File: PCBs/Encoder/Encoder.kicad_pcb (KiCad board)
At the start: 2 copper layers, 6 x 25 mm, 3 parts, among them J1 Conn_01x06_Male, U1 AS5047D

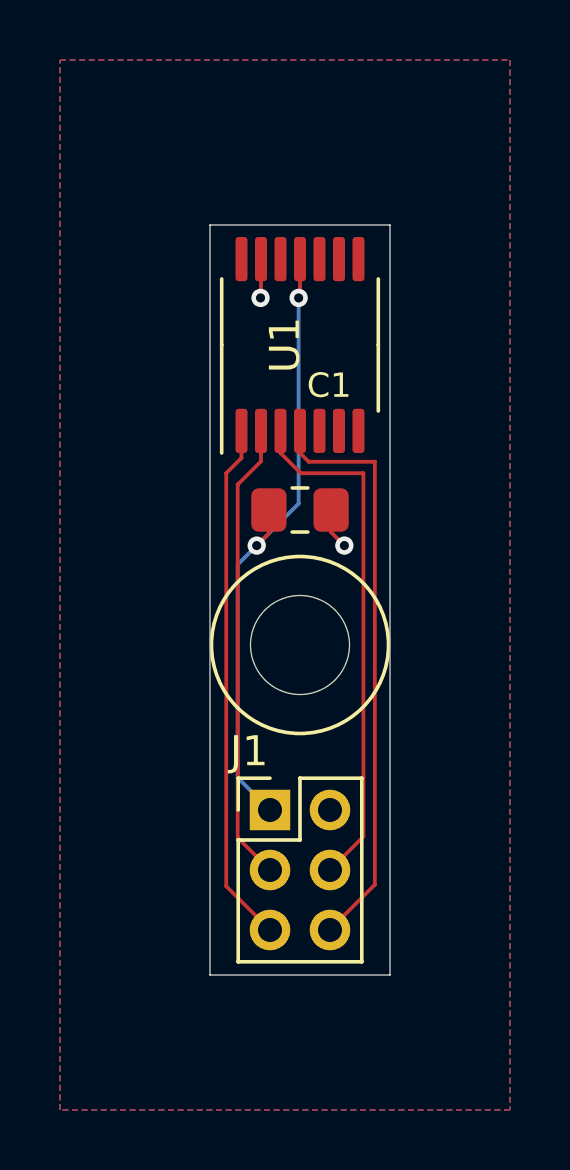
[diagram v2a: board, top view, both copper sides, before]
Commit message: encoder PCB update
datum relief and traces on bottom
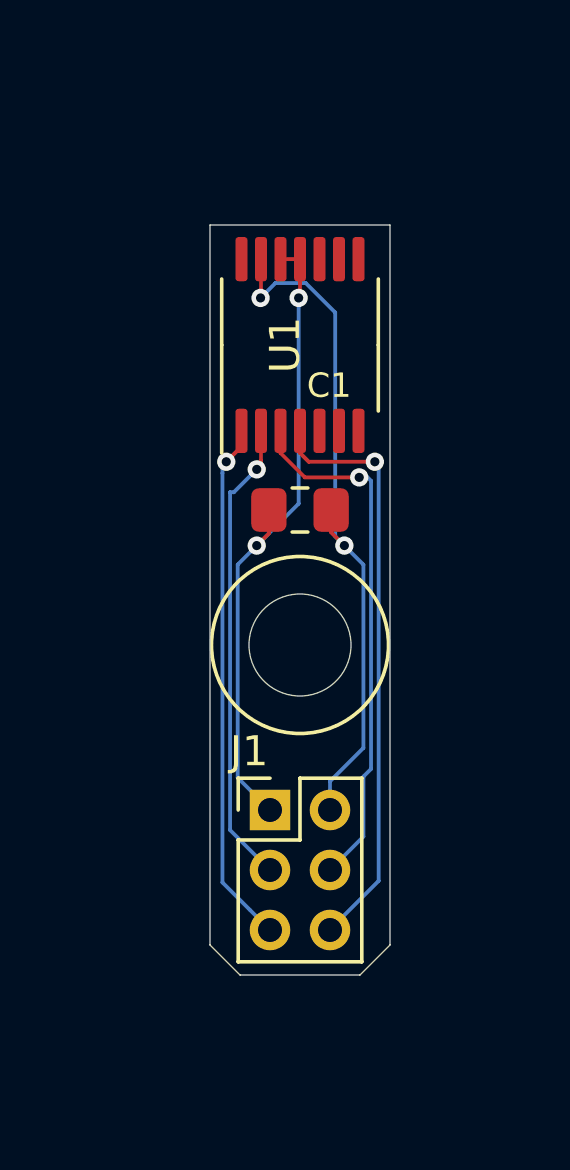
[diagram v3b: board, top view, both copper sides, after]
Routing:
- net GND: track 2.67 -> 23.2 mm
- net +3V3: track 21.0 -> 21.7 mm
- net CLK: track 15.4 -> 15.7 mm, vias 0 -> 1
- net MISO: track 17.5 -> 17.6 mm, vias 0 -> 1
- net CS: track 17.5 -> 17.6 mm, vias 0 -> 1
- net MOSI: track 19.6 -> 19.7 mm, vias 0 -> 1
- removed copper zone on F.Cu, net +3V3
- removed copper zone on B.Cu, net GND
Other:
- outline, holes or cut-outs redrawn
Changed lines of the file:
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@@
   (general
     (thickness 1.6)
-    (drawings 12)
-    (tracks 36)
+    (drawings 14)
+    (tracks 59)
     (zones 0)
     (modules 3)
@@
     (44 Edge.Cuts user)
     (45 Margin user)
-    (46 B.CrtYd user)
-    (47 F.CrtYd user)
+    (46 B.CrtYd user hide)
+    (47 F.CrtYd user hide)
     (48 B.Fab user hide)
     (49 F.Fab user)
@@
       (drillshape 0)
       (scaleselection 1)
-      (outputdirectory "/Output/"))
+      (outputdirectory "./Output/"))
   )
   (net 0 "")
@@
     )
   )
+  (gr_line (start 146 105.5) (end 145 104.5) (layer Edge.Cuts) (width 0.0254))
+  (gr_line (start 150 105.5) (end 151 104.5) (layer Edge.Cuts) (width 0.0254))
   (dimension 14 (width 0.15) (layer F.Fab)
     (gr_text "14.000 mm" (at 154.6152 87.5 90) (layer F.Fab)
@@
     (arrow2b (pts (xy 145 78.5) (xy 146.126504 77.913579)))
   )
-  (gr_line (start 145 105.5) (end 145 80.5) (layer Edge.Cuts) (width 0.0254))
-  (gr_line (start 151 105.5) (end 145 105.5) (layer Edge.Cuts) (width 0.0254))
-  (gr_line (start 151 80.5) (end 151 105.5) (layer Edge.Cuts) (width 0.0254))
+  (gr_line (start 145 104.5) (end 145 80.5) (layer Edge.Cuts) (width 0.0254))
+  (gr_line (start 150 105.5) (end 146 105.5) (layer Edge.Cuts) (width 0.0254))
+  (gr_line (start 151 80.5) (end 151 104.5) (layer Edge.Cuts) (width 0.0254))
   (gr_circle (center 148 94.5) (end 150.95 94.5) (layer F.SilkS) (width 0.12))
-  (gr_circle (center 148 94.5) (end 149.65 94.5) (layer Edge.Cuts) (width 0.0254))
+  (gr_circle (center 148 94.5) (end 149.7 94.5) (layer Edge.Cuts) (width 0.0254))
   (gr_line (start 145 80.5) (end 151 80.5) (layer Edge.Cuts) (width 0.0254))
   (via (at 146.685 82.931) (size 0.6096) (drill 0.3048) (layers F.Cu B.Cu) (net 1))
@@
   (segment (start 149.0375 90.7445) (end 149.479 91.186) (width 0.127) (layer F.Cu) (net 1))
   (segment (start 149.0375 90) (end 149.0375 90.7445) (width 0.127) (layer F.Cu) (net 1))
+  (segment (start 149.479 91.186) (end 150.114 91.821) (width 0.127) (layer B.Cu) (net 1))
+  (segment (start 149 99.045406) (end 149 100) (width 0.127) (layer B.Cu) (net 1))
+  (segment (start 150.114 97.931406) (end 149 99.045406) (width 0.127) (layer B.Cu) (net 1))
+  (segment (start 150.114 91.821) (end 150.114 97.931406) (width 0.127) (layer B.Cu) (net 1))
+  (segment (start 147.180301 82.435699) (end 146.685 82.931) (width 0.127) (layer B.Cu) (net 1))
+  (segment (start 148.192745 82.435699) (end 147.180301 82.435699) (width 0.127) (layer B.Cu) (net 1))
+  (segment (start 149.174201 83.417155) (end 148.192745 82.435699) (width 0.127) (layer B.Cu) (net 1))
+  (segment (start 149.174201 90.881201) (end 149.174201 83.417155) (width 0.127) (layer B.Cu) (net 1))
+  (segment (start 149.479 91.186) (end 149.174201 90.881201) (width 0.127) (layer B.Cu) (net 1))
   (via (at 147.955 82.931) (size 0.6096) (drill 0.3048) (layers F.Cu B.Cu) (net 2))
   (segment (start 148 82.886) (end 147.955 82.931) (width 0.127) (layer F.Cu) (net 2))
@@
   (segment (start 145.923 98.923) (end 147 100) (width 0.127) (layer B.Cu) (net 2))
   (segment (start 145.923 91.821) (end 145.923 98.923) (width 0.127) (layer B.Cu) (net 2))
-  (segment (start 146.05 87.3625) (end 146.05 88.265) (width 0.127) (layer F.Cu) (net 3))
-  (segment (start 146.05 88.265) (end 145.542 88.773) (width 0.127) (layer F.Cu) (net 3))
-  (segment (start 145.542 102.542) (end 147 104) (width 0.127) (layer F.Cu) (net 3))
-  (segment (start 145.542 88.773) (end 145.542 102.542) (width 0.127) (layer F.Cu) (net 3))
-  (segment (start 145.923 100.923) (end 147 102) (width 0.127) (layer F.Cu) (net 4))
-  (segment (start 145.923 89.154) (end 145.923 100.923) (width 0.127) (layer F.Cu) (net 4))
-  (segment (start 146.7 88.377) (end 145.923 89.154) (width 0.127) (layer F.Cu) (net 4))
+  (segment (start 147.35 81.6375) (end 148 81.6375) (width 0.127) (layer F.Cu) (net 2))
+  (segment (start 145.414989 102.414989) (end 146.325001 103.325001) (width 0.127) (layer B.Cu) (net 3))
+  (segment (start 146.325001 103.325001) (end 147 104) (width 0.127) (layer B.Cu) (net 3))
+  (via (at 145.542 88.392) (size 0.6096) (drill 0.3048) (layers F.Cu B.Cu) (net 3))
+  (segment (start 146.05 87.884) (end 145.542 88.392) (width 0.127) (layer F.Cu) (net 3))
+  (segment (start 146.05 87.3625) (end 146.05 87.884) (width 0.127) (layer F.Cu) (net 3))
+  (segment (start 145.414989 88.519011) (end 145.414989 88.773011) (width 0.127) (layer B.Cu) (net 3))
+  (segment (start 145.542 88.392) (end 145.414989 88.519011) (width 0.127) (layer B.Cu) (net 3))
+  (segment (start 145.414989 88.773011) (end 145.414989 102.414989) (width 0.127) (layer B.Cu) (net 3))
+  (segment (start 145.669 100.669) (end 147 102) (width 0.127) (layer B.Cu) (net 4))
+  (segment (start 145.669 89.408) (end 145.669 100.669) (width 0.127) (layer B.Cu) (net 4))
   (segment (start 146.7 87.3625) (end 146.7 88.377) (width 0.127) (layer F.Cu) (net 4))
-  (segment (start 150.114 88.773) (end 150.114 98.886) (width 0.127) (layer F.Cu) (net 5))
-  (segment (start 148.023 88.773) (end 150.114 88.773) (width 0.127) (layer F.Cu) (net 5))
-  (segment (start 147.35 88.1) (end 148.023 88.773) (width 0.127) (layer F.Cu) (net 5))
+  (via (at 146.558 88.646) (size 0.6096) (drill 0.3048) (layers F.Cu B.Cu) (net 4))
+  (segment (start 146.7 88.504) (end 146.558 88.646) (width 0.127) (layer F.Cu) (net 4))
+  (segment (start 146.7 88.377) (end 146.7 88.504) (width 0.127) (layer F.Cu) (net 4))
+  (segment (start 145.796 89.408) (end 145.669 89.408) (width 0.127) (layer B.Cu) (net 4))
+  (segment (start 146.558 88.646) (end 145.796 89.408) (width 0.127) (layer B.Cu) (net 4))
+  (via (at 149.974144 88.912856) (size 0.6096) (drill 0.3048) (layers F.Cu B.Cu) (net 5))
+  (segment (start 148.162856 88.912856) (end 149.974144 88.912856) (width 0.127) (layer F.Cu) (net 5))
+  (segment (start 147.35 88.1) (end 148.162856 88.912856) (width 0.127) (layer F.Cu) (net 5))
   (segment (start 147.35 87.3625) (end 147.35 88.1) (width 0.127) (layer F.Cu) (net 5))
-  (segment (start 150.114 100.886) (end 149 102) (width 0.127) (layer F.Cu) (net 5))
-  (segment (start 150.114 98.886) (end 150.114 100.886) (width 0.127) (layer F.Cu) (net 5))
-  (segment (start 150.495 102.489) (end 149 103.984) (width 0.127) (layer F.Cu) (net 6))
-  (segment (start 150.495 88.392) (end 150.495 102.489) (width 0.127) (layer F.Cu) (net 6))
-  (segment (start 148.292 88.392) (end 150.495 88.392) (width 0.127) (layer F.Cu) (net 6))
+  (segment (start 150.114 100.886) (end 149 102) (width 0.127) (layer B.Cu) (net 5))
+  (segment (start 150.114 98.886) (end 150.114 100.886) (width 0.127) (layer B.Cu) (net 5))
+  (segment (start 150.368 98.632) (end 150.114 98.886) (width 0.127) (layer B.Cu) (net 5))
+  (segment (start 150.368 89.027) (end 150.368 98.632) (width 0.127) (layer B.Cu) (net 5))
+  (segment (start 150.114 88.773) (end 150.368 89.027) (width 0.127) (layer B.Cu) (net 5))
   (segment (start 148 88.1) (end 148.292 88.392) (width 0.127) (layer F.Cu) (net 6))
   (segment (start 148 87.3625) (end 148 88.1) (width 0.127) (layer F.Cu) (net 6))
-  (zone (net 2) (net_name +3V3) (layer F.Cu) (hatch edge 0.508)
-    (connect_pads (clearance 0.254))
-    (min_thickness 0.127)
-    (fill yes (arc_segments 32) (thermal_gap 0.508) (thermal_bridge_width 0.508))
-    (polygon
-      (pts
-        (xy 155 110) (xy 140 110) (xy 140 75) (xy 155 75)
-      )
-    )
-  )
-  (zone (net 1) (net_name GND) (layer B.Cu) (hatch edge 0.508)
-    (connect_pads (clearance 0.254))
-    (min_thickness 0.254)
-    (fill yes (arc_segments 32) (thermal_gap 0.508) (thermal_bridge_width 0.508))
-    (polygon
-      (pts
-        (xy 155 110) (xy 140 110) (xy 140 75) (xy 155 75)
-      )
-    )
-  )
+  (via (at 150.495 88.392) (size 0.6096) (drill 0.3048) (layers F.Cu B.Cu) (net 6))
+  (segment (start 148.292 88.392) (end 150.495 88.392) (width 0.127) (layer F.Cu) (net 6))
+  (segment (start 150.622 102.362) (end 149 103.984) (width 0.127) (layer B.Cu) (net 6))
+  (segment (start 150.622 88.519) (end 150.622 102.362) (width 0.127) (layer B.Cu) (net 6))
+  (segment (start 150.495 88.392) (end 150.622 88.519) (width 0.127) (layer B.Cu) (net 6))
 )

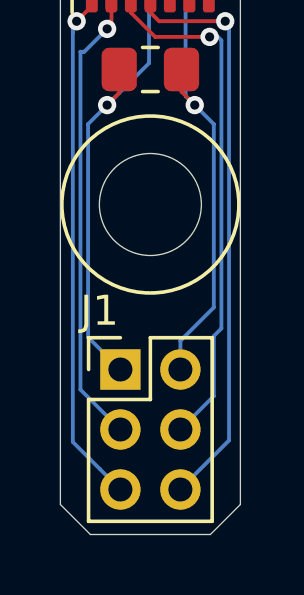
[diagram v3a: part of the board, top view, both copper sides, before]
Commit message: Encoder silkscreen update
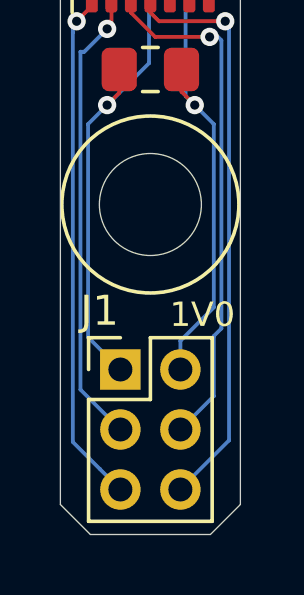
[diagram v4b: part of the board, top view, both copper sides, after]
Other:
- board text added: "1V0"
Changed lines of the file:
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@@
   (general
     (thickness 1.6)
-    (drawings 14)
+    (drawings 16)
     (tracks 59)
     (zones 0)
@@
       (effects (font (size 1 1) (thickness 0.15)))
     )
+    (fp_line (start 0 -1) (end 3 -1) (layer F.Fab) (width 0.1))
+    (fp_line (start 3 -1) (end 3 5) (layer F.Fab) (width 0.1))
+    (fp_line (start 3 5) (end -1 5) (layer F.Fab) (width 0.1))
+    (fp_line (start -1 5) (end -1 0) (layer F.Fab) (width 0.1))
+    (fp_line (start -1 0) (end 0 -1) (layer F.Fab) (width 0.1))
+    (fp_line (start -1.06 5.06) (end 3.06 5.06) (layer F.SilkS) (width 0.12))
+    (fp_line (start -1.06 1) (end -1.06 5.06) (layer F.SilkS) (width 0.12))
+    (fp_line (start 3.06 -1.06) (end 3.06 5.06) (layer F.SilkS) (width 0.12))
+    (fp_line (start -1.06 1) (end 1 1) (layer F.SilkS) (width 0.12))
+    (fp_line (start 1 1) (end 1 -1.06) (layer F.SilkS) (width 0.12))
+    (fp_line (start 1 -1.06) (end 3.06 -1.06) (layer F.SilkS) (width 0.12))
+    (fp_line (start -1.06 0) (end -1.06 -1.06) (layer F.SilkS) (width 0.12))
+    (fp_line (start -1.06 -1.06) (end 0 -1.06) (layer F.SilkS) (width 0.12))
+    (fp_line (start -1.5 -1.5) (end -1.5 5.5) (layer F.CrtYd) (width 0.05))
+    (fp_line (start -1.5 5.5) (end 3.5 5.5) (layer F.CrtYd) (width 0.05))
+    (fp_line (start 3.5 5.5) (end 3.5 -1.5) (layer F.CrtYd) (width 0.05))
     (fp_line (start 3.5 -1.5) (end -1.5 -1.5) (layer F.CrtYd) (width 0.05))
-    (fp_line (start 3.5 5.5) (end 3.5 -1.5) (layer F.CrtYd) (width 0.05))
-    (fp_line (start -1.5 5.5) (end 3.5 5.5) (layer F.CrtYd) (width 0.05))
-    (fp_line (start -1.5 -1.5) (end -1.5 5.5) (layer F.CrtYd) (width 0.05))
-    (fp_line (start -1.06 -1.06) (end 0 -1.06) (layer F.SilkS) (width 0.12))
-    (fp_line (start -1.06 0) (end -1.06 -1.06) (layer F.SilkS) (width 0.12))
-    (fp_line (start 1 -1.06) (end 3.06 -1.06) (layer F.SilkS) (width 0.12))
-    (fp_line (start 1 1) (end 1 -1.06) (layer F.SilkS) (width 0.12))
-    (fp_line (start -1.06 1) (end 1 1) (layer F.SilkS) (width 0.12))
-    (fp_line (start 3.06 -1.06) (end 3.06 5.06) (layer F.SilkS) (width 0.12))
-    (fp_line (start -1.06 1) (end -1.06 5.06) (layer F.SilkS) (width 0.12))
-    (fp_line (start -1.06 5.06) (end 3.06 5.06) (layer F.SilkS) (width 0.12))
-    (fp_line (start -1 0) (end 0 -1) (layer F.Fab) (width 0.1))
-    (fp_line (start -1 5) (end -1 0) (layer F.Fab) (width 0.1))
-    (fp_line (start 3 5) (end -1 5) (layer F.Fab) (width 0.1))
-    (fp_line (start 3 -1) (end 3 5) (layer F.Fab) (width 0.1))
-    (fp_line (start 0 -1) (end 3 -1) (layer F.Fab) (width 0.1))
     (fp_text user %R (at 1 2 90) (layer F.Fab)
       (effects (font (size 1 1) (thickness 0.15)))
@@
       (effects (font (size 1 1) (thickness 0.15)))
     )
+    (fp_line (start 0 2.61) (end 2.2 2.61) (layer F.SilkS) (width 0.12))
+    (fp_line (start 0 2.61) (end -2.2 2.61) (layer F.SilkS) (width 0.12))
+    (fp_line (start 0 -2.61) (end 2.2 -2.61) (layer F.SilkS) (width 0.12))
+    (fp_line (start 0 -2.61) (end -3.6 -2.61) (layer F.SilkS) (width 0.12))
+    (fp_line (start -1.2 -2.5) (end 2.2 -2.5) (layer F.Fab) (width 0.1))
+    (fp_line (start 2.2 -2.5) (end 2.2 2.5) (layer F.Fab) (width 0.1))
+    (fp_line (start 2.2 2.5) (end -2.2 2.5) (layer F.Fab) (width 0.1))
+    (fp_line (start -2.2 2.5) (end -2.2 -1.5) (layer F.Fab) (width 0.1))
+    (fp_line (start -2.2 -1.5) (end -1.2 -2.5) (layer F.Fab) (width 0.1))
+    (fp_line (start -3.85 -2.75) (end -3.85 2.75) (layer F.CrtYd) (width 0.05))
+    (fp_line (start -3.85 2.75) (end 3.85 2.75) (layer F.CrtYd) (width 0.05))
+    (fp_line (start 3.85 2.75) (end 3.85 -2.75) (layer F.CrtYd) (width 0.05))
     (fp_line (start 3.85 -2.75) (end -3.85 -2.75) (layer F.CrtYd) (width 0.05))
-    (fp_line (start 3.85 2.75) (end 3.85 -2.75) (layer F.CrtYd) (width 0.05))
-    (fp_line (start -3.85 2.75) (end 3.85 2.75) (layer F.CrtYd) (width 0.05))
-    (fp_line (start -3.85 -2.75) (end -3.85 2.75) (layer F.CrtYd) (width 0.05))
-    (fp_line (start -2.2 -1.5) (end -1.2 -2.5) (layer F.Fab) (width 0.1))
-    (fp_line (start -2.2 2.5) (end -2.2 -1.5) (layer F.Fab) (width 0.1))
-    (fp_line (start 2.2 2.5) (end -2.2 2.5) (layer F.Fab) (width 0.1))
-    (fp_line (start 2.2 -2.5) (end 2.2 2.5) (layer F.Fab) (width 0.1))
-    (fp_line (start -1.2 -2.5) (end 2.2 -2.5) (layer F.Fab) (width 0.1))
-    (fp_line (start 0 -2.61) (end -3.6 -2.61) (layer F.SilkS) (width 0.12))
-    (fp_line (start 0 -2.61) (end 2.2 -2.61) (layer F.SilkS) (width 0.12))
-    (fp_line (start 0 2.61) (end -2.2 2.61) (layer F.SilkS) (width 0.12))
-    (fp_line (start 0 2.61) (end 2.2 2.61) (layer F.SilkS) (width 0.12))
     (fp_text user %R (at 0 0 90) (layer F.Fab)
       (effects (font (size 1 1) (thickness 0.15)))
@@
       (effects (font (size 1 1) (thickness 0.15)))
     )
+    (fp_line (start -1 0.625) (end -1 -0.625) (layer F.Fab) (width 0.1))
+    (fp_line (start -1 -0.625) (end 1 -0.625) (layer F.Fab) (width 0.1))
+    (fp_line (start 1 -0.625) (end 1 0.625) (layer F.Fab) (width 0.1))
+    (fp_line (start 1 0.625) (end -1 0.625) (layer F.Fab) (width 0.1))
+    (fp_line (start -0.261252 -0.735) (end 0.261252 -0.735) (layer F.SilkS) (width 0.12))
+    (fp_line (start -0.261252 0.735) (end 0.261252 0.735) (layer F.SilkS) (width 0.12))
+    (fp_line (start -1.88 0.98) (end -1.88 -0.98) (layer F.CrtYd) (width 0.05))
+    (fp_line (start -1.88 -0.98) (end 1.88 -0.98) (layer F.CrtYd) (width 0.05))
+    (fp_line (start 1.88 -0.98) (end 1.88 0.98) (layer F.CrtYd) (width 0.05))
     (fp_line (start 1.88 0.98) (end -1.88 0.98) (layer F.CrtYd) (width 0.05))
-    (fp_line (start 1.88 -0.98) (end 1.88 0.98) (layer F.CrtYd) (width 0.05))
-    (fp_line (start -1.88 -0.98) (end 1.88 -0.98) (layer F.CrtYd) (width 0.05))
-    (fp_line (start -1.88 0.98) (end -1.88 -0.98) (layer F.CrtYd) (width 0.05))
-    (fp_line (start -0.261252 0.735) (end 0.261252 0.735) (layer F.SilkS) (width 0.12))
-    (fp_line (start -0.261252 -0.735) (end 0.261252 -0.735) (layer F.SilkS) (width 0.12))
-    (fp_line (start 1 0.625) (end -1 0.625) (layer F.Fab) (width 0.1))
-    (fp_line (start 1 -0.625) (end 1 0.625) (layer F.Fab) (width 0.1))
-    (fp_line (start -1 -0.625) (end 1 -0.625) (layer F.Fab) (width 0.1))
-    (fp_line (start -1 0.625) (end -1 -0.625) (layer F.Fab) (width 0.1))
     (fp_text user %R (at 0 0) (layer F.Fab)
       (effects (font (size 0.5 0.5) (thickness 0.08)))
@@
     )
   )
+  (gr_text 1V0 (at 149.733 98.171 180) (layer B.SilkS)
+    (effects (font (size 0.8128 0.8128) (thickness 0.1524)) (justify mirror))
+  )
+  (gr_text 1V0 (at 149.733 98.171) (layer F.SilkS)
+    (effects (font (size 0.8128 0.8128) (thickness 0.1524)))
+  )
   (gr_line (start 146 105.5) (end 145 104.5) (layer Edge.Cuts) (width 0.0254))
